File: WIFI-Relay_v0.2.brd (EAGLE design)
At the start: 49.2 x 44.4 mm, 38 parts, among them CN1 PBS-3-VERTICAL, CN2 PBS-2-VERTICAL, CN3 PBS-8-1.27-VERTICAL, CN4 PBS-8-1.27-VERTICAL, CN5 PBS-2-VERTICAL, CN6 PBS-2-VERTICAL, CN7 PBS-4-VERTICAL, IC1 74LS595D, IC2 74LS595D, IC3 MC34063AD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

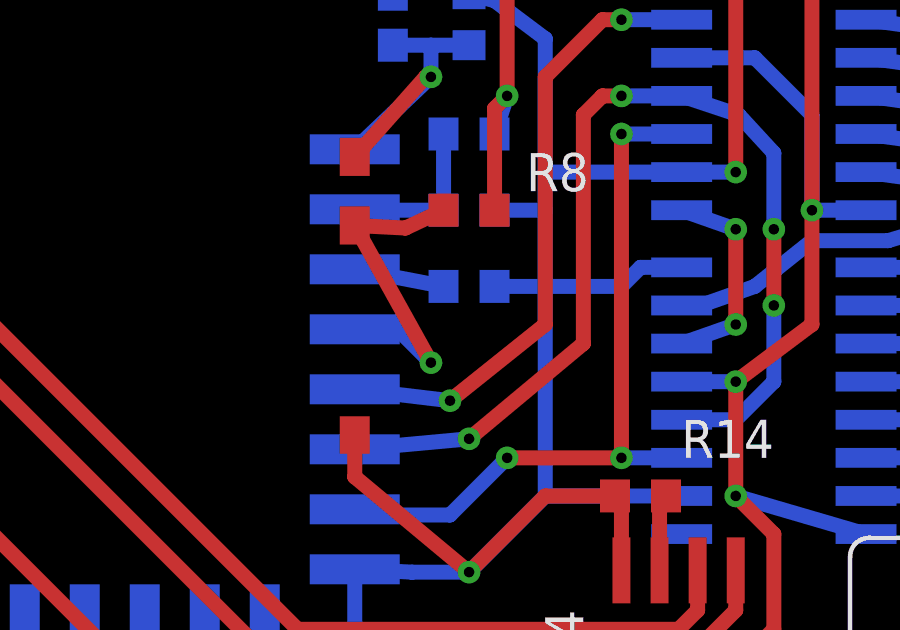
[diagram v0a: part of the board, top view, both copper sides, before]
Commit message: Button "Reset settings" was replaced with N$27
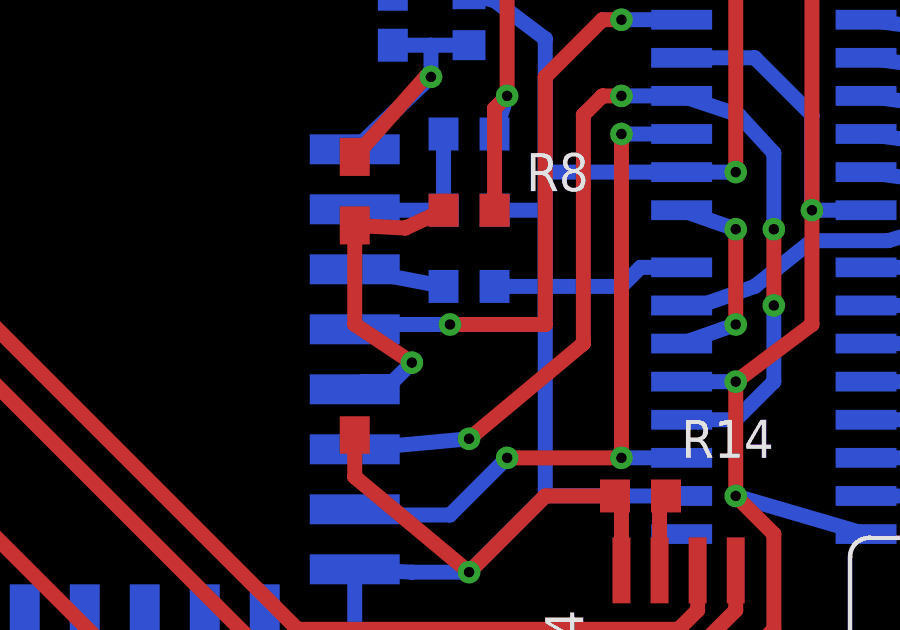
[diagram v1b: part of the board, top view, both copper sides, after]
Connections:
- net N$27: now also M1.G16; no longer M1.G14
- net RST: now also M1.G14; no longer M1.G16
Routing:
- net N$27: track 20.9 -> 20.0 mm
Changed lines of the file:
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@@
 <layer number="27" name="tValues" color="7" fill="1" visible="yes" active="yes"/>
 <layer number="28" name="bValues" color="7" fill="1" visible="yes" active="yes"/>
-<layer number="29" name="tStop" color="7" fill="3" visible="yes" active="yes"/>
-<layer number="30" name="bStop" color="7" fill="6" visible="yes" active="yes"/>
+<layer number="29" name="tStop" color="7" fill="3" visible="no" active="yes"/>
+<layer number="30" name="bStop" color="7" fill="6" visible="no" active="yes"/>
 <layer number="31" name="tCream" color="7" fill="4" visible="no" active="yes"/>
 <layer number="32" name="bCream" color="7" fill="5" visible="no" active="yes"/>
@@
 <signal name="N$27">
 <contactref element="IC1" pad="14"/>
-<contactref element="M1" pad="G14"/>
-<wire x1="25.4" y1="25.145" x2="28.575" y2="24.765" width="0.5" layer="16"/>
-<wire x1="28.575" y1="24.765" x2="31.75" y2="27.305" width="0.5" layer="1"/>
+<wire x1="28.575" y1="27.305" x2="31.75" y2="27.305" width="0.5" layer="1"/>
 <wire x1="31.75" y1="27.305" x2="31.75" y2="35.56" width="0.5" layer="1"/>
 <wire x1="31.75" y1="35.56" x2="33.655" y2="37.465" width="0.5" layer="1"/>
@@
 <wire x1="34.29" y1="37.465" x2="36.2966" y2="37.465" width="0.5" layer="16"/>
 <via x="34.29" y="37.465" extent="1-16" drill="0.35"/>
-<via x="28.575" y="24.765" extent="1-16" drill="0.35"/>
+<via x="28.575" y="27.305" extent="1-16" drill="0.35"/>
+<contactref element="M1" pad="G16"/>
+<wire x1="28.575" y1="27.305" x2="25.56" y2="27.305" width="0.5" layer="16"/>
+<wire x1="25.56" y1="27.305" x2="25.4" y2="27.145" width="0.5" layer="16"/>
 </signal>
 <signal name="RCK">
@@
 </signal>
 <signal name="RST">
-<contactref element="M1" pad="G16"/>
 <contactref element="R8" pad="1"/>
 <contactref element="BTN1" pad="2"/>
-<wire x1="25.4" y1="27.145" x2="26.83" y2="27.145" width="0.5" layer="16"/>
-<wire x1="26.83" y1="27.145" x2="27.94" y2="26.035" width="0.5" layer="16"/>
-<via x="27.94" y="26.035" extent="1-16" drill="0.35"/>
-<wire x1="27.94" y1="26.035" x2="25.4" y2="30.607" width="0.5" layer="1"/>
+<wire x1="27.305" y1="26.035" x2="26.67" y2="25.4" width="0.5" layer="16"/>
+<via x="27.305" y="26.035" extent="1-16" drill="0.35"/>
+<wire x1="27.305" y1="26.035" x2="25.4" y2="27.305" width="0.5" layer="1"/>
+<wire x1="25.4" y1="27.305" x2="25.4" y2="30.607" width="0.5" layer="1"/>
 <wire x1="28.36" y1="31.115" x2="27.09" y2="30.52" width="0.5" layer="1"/>
 <wire x1="27.09" y1="30.52" x2="25.4" y2="30.607" width="0.5" layer="1"/>
+<contactref element="M1" pad="G14"/>
+<wire x1="26.67" y1="25.4" x2="25.655" y2="25.4" width="0.5" layer="16"/>
+<wire x1="25.655" y1="25.4" x2="25.4" y2="25.145" width="0.5" layer="16"/>
 </signal>
 <signal name="N$30">
